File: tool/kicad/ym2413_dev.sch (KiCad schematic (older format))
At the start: 86 parts, among them P1 CONN_4, U1 YM2413, X1 CRYSTAL

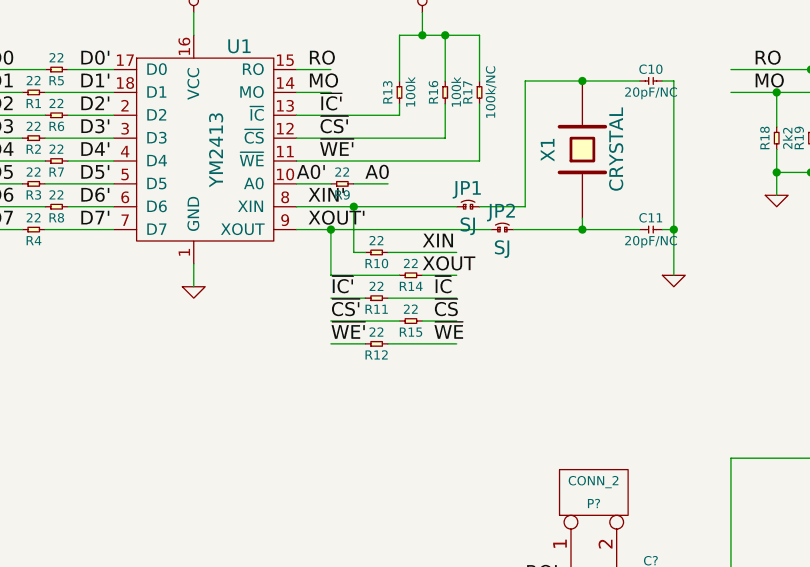
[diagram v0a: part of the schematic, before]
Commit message: add extra solder jumpers for XIN/XOUT handling on YM
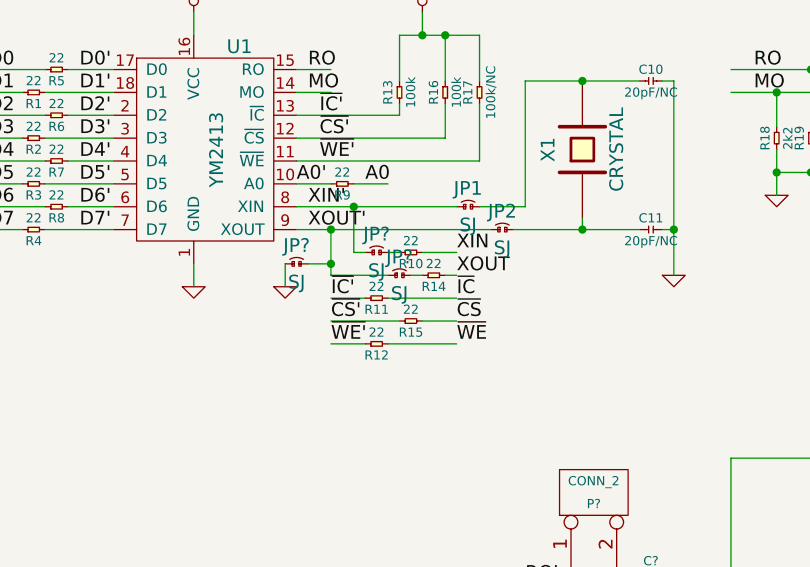
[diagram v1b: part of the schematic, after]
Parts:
- added JP? (x3): SJ, symbol SJ
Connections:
- wire segments 241 -> 245
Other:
- moved on the sheet: R10, R14
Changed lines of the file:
@@
 L R R10
 U 1 1 52E3BD6F
-P 6900 2400
-F 0 "R10" H 6900 2450 40  0000 C CNN
-F 1 "22" H 6900 2350 40  0000 C CNN
-F 2 "" H 6900 2400 60  0000 C CNN
-F 3 "" H 6900 2400 60  0000 C CNN
-	1    6900 2400
+P 7050 2400
+F 0 "R10" H 7050 2450 40  0000 C CNN
+F 1 "22" H 7050 2350 40  0000 C CNN
+F 2 "" H 7050 2400 60  0000 C CNN
+F 3 "" H 7050 2400 60  0000 C CNN
+	1    7050 2400
 	-1   0    0    1
 $EndComp
@@
 L R R14
 U 1 1 52E3BD75
-P 7050 2500
-F 0 "R14" H 7050 2550 40  0000 C CNN
-F 1 "22" H 7050 2450 40  0000 C CNN
-F 2 "" H 7050 2500 60  0000 C CNN
-F 3 "" H 7050 2500 60  0000 C CNN
-	1    7050 2500
+P 7150 2500
+F 0 "R14" H 7150 2550 40  0000 C CNN
+F 1 "22" H 7150 2450 40  0000 C CNN
+F 2 "" H 7150 2500 60  0000 C CNN
+F 3 "" H 7150 2500 60  0000 C CNN
+	1    7150 2500
 	-1   0    0    1
 $EndComp
-Text Label 7100 2400 0    60   ~ 0
+Text Label 7250 2400 0    60   ~ 0
 XIN
-Text Label 7100 2500 0    60   ~ 0
+Text Label 7250 2500 0    60   ~ 0
 XOUT
 $Comp
@@
 	-1   0    0    1
 $EndComp
-Text Label 7150 2600 0    60   ~ 0
+Text Label 7250 2600 0    60   ~ 0
 ~IC
-Text Label 7150 2700 0    60   ~ 0
+Text Label 7250 2700 0    60   ~ 0
 ~CS
-Text Label 7150 2800 0    60   ~ 0
+Text Label 7250 2800 0    60   ~ 0
 ~WE
 Text Label 6700 2800 0    60   ~ 0
@@
 	6950 2100 6800 2100
 Wire Wire Line
-	6850 2400 6800 2400
-Wire Wire Line
 	6800 2400 6800 2200
 Connection ~ 6800 2200
 Wire Wire Line
-	7000 2500 6700 2500
-Wire Wire Line
 	6700 2500 6700 2300
 Connection ~ 6700 2300
-Wire Wire Line
-	6950 2400 7250 2400
-Wire Wire Line
-	7250 2500 7100 2500
 Wire Wire Line
 	7250 2600 6950 2600
@@
 	4400 7350 4400 7400
 Connection ~ 4400 7400
+Wire Wire Line
+	7100 2400 7250 2400
+Wire Wire Line
+	7250 2500 7200 2500
+$Comp
+L SJ JP?
+U 1 1 52F78C85
+P 6900 2400
+F 0 "JP?" H 6900 2480 60  0000 C CNN
+F 1 "SJ" H 6900 2320 60  0000 C CNN
+F 2 "" H 6900 2400 60  0000 C CNN
+F 3 "" H 6900 2400 60  0000 C CNN
+	1    6900 2400
+	1    0    0    -1
+$EndComp
+$Comp
+L SJ JP?
+U 1 1 52F78C8B
+P 7000 2500
+F 0 "JP?" H 7000 2580 60  0000 C CNN
+F 1 "SJ" H 7000 2420 60  0000 C CNN
+F 2 "" H 7000 2500 60  0000 C CNN
+F 3 "" H 7000 2500 60  0000 C CNN
+	1    7000 2500
+	1    0    0    -1
+$EndComp
+Wire Wire Line
+	7100 2500 7050 2500
+Wire Wire Line
+	6950 2500 6700 2500
+Wire Wire Line
+	7000 2400 6950 2400
+Wire Wire Line
+	6850 2400 6800 2400
+$Comp
+L GND #PWR?
+U 1 1 52F7930D
+P 6500 2550
+F 0 "#PWR?" H 6500 2550 30  0001 C CNN
+F 1 "GND" H 6500 2480 30  0001 C CNN
+F 2 "" H 6500 2550 60  0000 C CNN
+F 3 "" H 6500 2550 60  0000 C CNN
+	1    6500 2550
+	1    0    0    -1
+$EndComp
+$Comp
+L SJ JP?
+U 1 1 52F79313
+P 6550 2450
+F 0 "JP?" H 6550 2530 60  0000 C CNN
+F 1 "SJ" H 6550 2370 60  0000 C CNN
+F 2 "" H 6550 2450 60  0000 C CNN
+F 3 "" H 6550 2450 60  0000 C CNN
+	1    6550 2450
+	1    0    0    -1
+$EndComp
+Wire Wire Line
+	6700 2450 6600 2450
+Connection ~ 6700 2450
+Wire Wire Line
+	6500 2450 6500 2550
 $EndSCHEMATC

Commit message: add SWC pull-up button to enable bootloader programming
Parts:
- added R?: 100, symbol R
- added S?: TACTSW, symbol TACTSW
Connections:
- wire segments 245 -> 249
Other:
- moved on the sheet: C?, P?, R?, U?

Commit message: add fast lvl shifer IC to make sure we provide a 5V clock on XI
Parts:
- removed P? (x2): CONN_2, symbol CONN_2
- added K?: CONN_3, symbol CONN_3
- added U?: SN74LVC2T45, symbol SN74LVC2T45
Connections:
- net labels added: XIN3V3, XOUT3V3
- wire segments 249 -> 268
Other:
- note added: "TODO: actual audio\nconnector"
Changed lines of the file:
@@
-$EndComp
-$Comp
-L CONN_2 P?
-U 1 1 52F742B0
-P 10650 3350
-F 0 "P?" V 10600 3350 40  0000 C CNN
-F 1 "CONN_2" V 10700 3350 40  0000 C CNN
-F 2 "" H 10650 3350 60  0000 C CNN
-F 3 "" H 10650 3350 60  0000 C CNN
-	1    10650 3350
-	1    0    0    -1
 $EndComp
 $Comp
@@
 $EndComp
 $Comp
-L CONN_2 P?
-U 1 1 52F7492B
-P 10650 4600
-F 0 "P?" V 10600 4600 40  0000 C CNN
-F 1 "CONN_2" V 10700 4600 40  0000 C CNN
-F 2 "" H 10650 4600 60  0000 C CNN
-F 3 "" H 10650 4600 60  0000 C CNN
-	1    10650 4600
-	1    0    0    -1
-$EndComp
-$Comp
 L GND #PWR?
 U 1 1 52F74931
@@
 	9950 3250 10050 3250
 Wire Wire Line
-	10150 3250 10300 3250
+	10150 3250 10400 3250
 Wire Wire Line
 	10200 3400 10200 3250
@@
 Wire Wire Line
 	8800 5550 8800 5650
+$Comp
+L CONN_3 K?
+U 1 1 52F7A1A7
+P 10850 3950
+F 0 "K?" V 10800 3950 50  0000 C CNN
+F 1 "CONN_3" V 10900 3950 40  0000 C CNN
+F 2 "" H 10850 3950 60  0000 C CNN
+F 3 "" H 10850 3950 60  0000 C CNN
+	1    10850 3950
+	1    0    0    -1
+$EndComp
+Wire Wire Line
+	10500 3850 10400 3850
+Wire Wire Line
+	10400 3850 10400 3250
+Wire Wire Line
+	10300 4500 10300 3950
+Wire Wire Line
+	10300 3950 10500 3950
+$Comp
+L GND #PWR?
+U 1 1 52F7A44E
+P 10400 4150
+F 0 "#PWR?" H 10400 4150 30  0001 C CNN
+F 1 "GND" H 10400 4080 30  0001 C CNN
+F 2 "" H 10400 4150 60  0000 C CNN
+F 3 "" H 10400 4150 60  0000 C CNN
+	1    10400 4150
+	1    0    0    -1
+$EndComp
+Wire Wire Line
+	10500 4050 10400 4050
+Wire Wire Line
+	10400 4050 10400 4150
+Text Notes 10700 5000 1    60   ~ 0
+TODO: actual audio\nconnector
+$Comp
+L SN74LVC2T45 U?
+U 1 1 52F7A857
+P 1450 4100
+F 0 "U?" H 1450 4450 60  0000 C CNN
+F 1 "SN74LVC2T45" H 1450 3800 60  0000 C CNN
+F 2 "" H 1500 3950 60  0000 C CNN
+F 3 "" H 1500 3950 60  0000 C CNN
+	1    1450 4100
+	-1   0    0    -1
+$EndComp
+$Comp
+L +3.3V #PWR?
+U 1 1 52F7A870
+P 1900 3750
+F 0 "#PWR?" H 1900 3710 30  0001 C CNN
+F 1 "+3.3V" H 1900 3860 30  0000 C CNN
+F 2 "" H 1900 3750 60  0000 C CNN
+F 3 "" H 1900 3750 60  0000 C CNN
+	1    1900 3750
+	1    0    0    -1
+$EndComp
+Wire Wire Line
+	1800 3900 1900 3900
+Wire Wire Line
+	1900 3750 1900 4000
+Wire Wire Line
+	1900 4000 1800 4000
+Connection ~ 1900 3900
+Wire Wire Line
+	1800 4100 2000 4100
+Wire Wire Line
+	2000 4100 2000 3900
+Wire Wire Line
+	2000 3900 2850 3900
+Wire Wire Line
+	1800 4200 2050 4200
+Wire Wire Line
+	2050 4200 2050 4000
+Wire Wire Line
+	2050 4000 2850 4000
+Wire Wire Line
+	950  4100 1100 4100
+Wire Wire Line
+	950  4200 1100 4200
+Wire Wire Line
+	1100 3900 950  3900
+Wire Wire Line
+	950  3900 950  3800
+$Comp
+L +5V #PWR?
+U 1 1 52F7B2D9
+P 950 3800
+F 0 "#PWR?" H 950 3890 20  0001 C CNN
+F 1 "+5V" H 950 3890 30  0000 C CNN
+F 2 "" H 950 3800 60  0000 C CNN
+F 3 "" H 950 3800 60  0000 C CNN
+	1    950  3800
+	1    0    0    -1
+$EndComp
+Text Label 1000 4100 2    60   ~ 0
+XIN
+Text Label 1000 4200 2    60   ~ 0
+XOUT
+Text Label 2050 3900 0    60   ~ 0
+XIN3V3
+Text Label 2050 4000 0    60   ~ 0
+XOUT3V3
 $EndSCHEMATC

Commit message: cleanup; assign pins; add test points; restart pcb layout from zero
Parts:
- added D1, D10, D11, D2, D3, D4, D5, D6, D7, D8, D9: LED, symbol LED
- added K1: CONN_3, symbol CONN_3
- added P1, P10, P11, P12, P13, P14, P15, P16, P17, P18, P19, P2, P20, P21, P22, P23, P24, P25, P26, P27, P28, P29, P3, P33, P34, P4, P6, P7, P8, P9: TEST_POINT, symbol TEST_POINT
- added R1, R10, R13, R2, R3, R4, R5, R6, R7, R8, R9: 3k3, symbol R
- added R25, R26, R27: 22, symbol R
- IC1: renamed from IC?; footprint DIP8 -> (none)
- P5: renamed from P?; value MINI-IN -> MIDI-IN
- gave numbers to parts that had none: 55
- renumbered C10 to C15, C11 to C16, C1 to C18, C2 to C19, JP1 to JP4, JP2 to JP5, P1 to P35, R1 to R17, R2 to R18, R3 to R19, R4 to R20, R5 to R21, R6 to R22, R7 to R23, R8 to R24, R9 to R28, R11 to R29, R12 to R30, R13 to R31, R10 to R32, R15 to R33, R14 to R34, R16 to R35, R17 to R36, R18 to R40, R19 to R41, R20 to R43, R21 to R44, R22 to R45, R23 to R46, R24 to R47, R25 to R50, U1 to U4, X1 to X2
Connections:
- net labels added: DEBUG_RX, DEBUG_TX, LED0, LED1, LED2, LED3, LED4, LED5, LED6, LED7, LED8, LED9, USB_DMPU
- wire segments 268 -> 351
- no-connect marks 3 -> 4

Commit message: add 6-pin FTDI debug header
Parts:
- removed P35: CONN_4, symbol CONN_4
- added P35: CONN_6, symbol CONN_6
- added P36: CONN_5, symbol CONN_5
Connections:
- net labels added: RXI, TXO
- wire segments 351 -> 360
- no-connect marks 4 -> 5
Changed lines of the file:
@@
 MO/2
 $Comp
-L CONN_4 P35
-U 1 1 52E3A865
-P 10750 1750
-F 0 "P35" V 10700 1750 50  0000 C CNN
-F 1 "CONN_4" V 10800 1750 50  0000 C CNN
-F 2 "" H 10750 1750 60  0000 C CNN
-F 3 "" H 10750 1750 60  0000 C CNN
-	1    10750 1750
-	1    0    0    -1
-$EndComp
-$Comp
 L R R40
 U 1 1 52E3AC6B
@@
 	0    -1   -1   0
 $EndComp
+$Comp
+L CONN_5 P36
+U 1 1 52F868F0
+P 10800 1700
+F 0 "P36" V 10750 1700 50  0000 C CNN
+F 1 "CONN_5" V 10850 1700 50  0000 C CNN
+F 2 "" H 10800 1700 60  0000 C CNN
+F 3 "" H 10800 1700 60  0000 C CNN
+	1    10800 1700
+	1    0    0    -1
+$EndComp
+Wire Wire Line
+	10400 1500 10350 1500
+Wire Wire Line
+	10350 1500 10350 1900
+Connection ~ 10350 1900
+$Comp
+L CONN_6 P35
+U 1 1 52F86C85
+P 6400 6700
+F 0 "P35" V 6350 6700 60  0000 C CNN
+F 1 "CONN_6" V 6450 6700 60  0000 C CNN
+F 2 "" H 6400 6700 60  0000 C CNN
+F 3 "" H 6400 6700 60  0000 C CNN
+	1    6400 6700
+	1    0    0    -1
+$EndComp
+Wire Wire Line
+	6050 6450 6000 6450
+Wire Wire Line
+	6000 6450 6000 6850
+Wire Wire Line
+	6000 6850 6050 6850
+Wire Wire Line
+	5600 6550 6050 6550
+Wire Wire Line
+	5600 6650 6050 6650
+Wire Wire Line
+	5900 6950 6050 6950
+$Comp
+L GND #PWR056
+U 1 1 52F8750B
+P 5900 7050
+F 0 "#PWR056" H 5900 7050 30  0001 C CNN
+F 1 "GND" H 5900 6980 30  0001 C CNN
+F 2 "" H 5900 7050 60  0000 C CNN
+F 3 "" H 5900 7050 60  0000 C CNN
+	1    5900 7050
+	1    0    0    -1
+$EndComp
+Wire Wire Line
+	5900 6950 5900 7050
+NoConn ~ 6050 6750
+Text Label 5950 6650 2    60   ~ 0
+TXO
+Text Label 5950 6550 2    60   ~ 0
+RXI
+Text Label 5750 6550 2    60   ~ 0
+DEBUG_TX
+Text Label 5750 6650 2    60   ~ 0
+DEBUG_RX
 $EndSCHEMATC

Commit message: rough layout
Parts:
- removed R29, R30, R33: 22, symbol R
- added P37, P38: TEST_POINT, symbol TEST_POINT
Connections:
- net labels added: MOA, MOA2, MOA3, MOI2, ROA, ROA2, ROA3, ROI2
- wire segments 360 -> 362
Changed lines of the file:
@@
 XOUT
-$Comp
-L R R29
-U 1 1 52E3BF37
-P 6900 2600
-F 0 "R29" H 6900 2650 40  0000 C CNN
-F 1 "22" H 6900 2550 40  0000 C CNN
-F 2 "" H 6900 2600 60  0000 C CNN
-F 3 "" H 6900 2600 60  0000 C CNN
-	1    6900 2600
-	-1   0    0    1
-$EndComp
-$Comp
-L R R33
-U 1 1 52E3BFF3
-P 7050 2700
-F 0 "R33" H 7050 2750 40  0000 C CNN
-F 1 "22" H 7050 2650 40  0000 C CNN
-F 2 "" H 7050 2700 60  0000 C CNN
-F 3 "" H 7050 2700 60  0000 C CNN
-	1    7050 2700
-	-1   0    0    1
-$EndComp
-$Comp
-L R R30
-U 1 1 52E3BFF9
-P 6900 2800
-F 0 "R30" H 6900 2850 40  0000 C CNN
-F 1 "22" H 6900 2750 40  0000 C CNN
-F 2 "" H 6900 2800 60  0000 C CNN
-F 3 "" H 6900 2800 60  0000 C CNN
-	1    6900 2800
-	-1   0    0    1
-$EndComp
-Text Label 7250 2600 0    60   ~ 0
-~IC
-Text Label 7250 2700 0    60   ~ 0
-~CS
-Text Label 7250 2800 0    60   ~ 0
-~WE
-Text Label 6700 2800 0    60   ~ 0
-~WE'
-Text Label 6700 2700 0    60   ~ 0
-~CS'
-Text Label 6700 2600 0    60   ~ 0
-~IC'
 $Comp
 L SJ JP5
@@
 L +3.3VADC #PWR014
 U 1 1 52F431B2
-P 3450 2450
-F 0 "#PWR014" H 3450 2570 20  0001 C CNN
-F 1 "+3.3VADC" H 3450 2540 30  0000 C CNN
-F 2 "" H 3450 2450 60  0000 C CNN
-F 3 "" H 3450 2450 60  0000 C CNN
-	1    3450 2450
+P 3450 2500
+F 0 "#PWR014" H 3450 2620 20  0001 C CNN
+F 1 "+3.3VADC" H 3450 2590 30  0000 C CNN
+F 2 "" H 3450 2500 60  0000 C CNN
+F 3 "" H 3450 2500 60  0000 C CNN
+	1    3450 2500
 	1    0    0    -1
 $EndComp
@@
 F 3 "" H 2800 6700 60  0000 C CNN
 	1    2800 6700
-	1    0    0    -1
+	-1   0    0    1
 $EndComp
 NoConn ~ 1600 6750
@@
 	1    0    0    -1
 $EndComp
-Text Label 3600 6650 0    60   ~ 0
+Text Label 3950 6500 1    60   ~ 0
 D-
-Text Label 3600 6750 0    60   ~ 0
+Text Label 4050 6500 1    60   ~ 0
 D+
 $Comp
@@
 Text Label 1850 6400 0    60   ~ 0
 VBUS_IN
-Text Label 1850 6650 0    60   ~ 0
+Text Label 2150 6750 0    60   ~ 0
 D-_IN
-Text Label 1900 6700 3    60   ~ 0
+Text Label 2150 6650 0    60   ~ 0
 D+_IN
 Text Label 1650 7050 1    60   ~ 0
@@
 	1    0    0    -1
 $EndComp
+Text Label 3150 6750 0    60   ~ 0
+D-B
 Text Label 3150 6650 0    60   ~ 0
-D-B
-Text Label 3150 6750 0    60   ~ 0
 D+B
 $Comp
@@
 Connection ~ 6700 2300
 Wire Wire Line
-	7250 2600 6950 2600
-Wire Wire Line
-	7250 2700 7100 2700
-Wire Wire Line
-	7250 2800 6950 2800
-Wire Wire Line
-	6850 2600 6700 2600
-Wire Wire Line
-	6700 2700 7000 2700
-Wire Wire Line
-	6700 2800 6850 2800
-Wire Wire Line
 	3250 5850 3250 5600
 Wire Wire Line
@@
 	1650 7250 1650 7300
 Wire Wire Line
-	1600 6650 2450 6650
-Wire Wire Line
-	1600 6700 2400 6700
-Wire Wire Line
-	2400 6700 2400 6750
-Wire Wire Line
-	2400 6750 2450 6750
-Wire Wire Line
 	1700 6400 1700 6600
 Wire Wire Line
@@
 	1700 6400 3050 6400
 Wire Wire Line
-	2750 6400 2750 6450
-Wire Wire Line
-	2850 6950 2850 7050
-Wire Wire Line
 	3150 6650 3350 6650
 Wire Wire Line
@@
 Wire Wire Line
 	3300 6400 3150 6400
-Connection ~ 2750 6400
 Wire Wire Line
 	3300 6350 3300 6400
-Wire Wire Line
-	3450 6650 4050 6650
-Wire Wire Line
-	3550 6750 3950 6750
 Wire Wire Line
 	4050 2900 4050 2450
@@
 Connection ~ 1900 3900
 Wire Wire Line
-	1800 4100 2000 4100
-Wire Wire Line
-	2000 4100 2000 3900
+	2000 3900 2000 4200
 Wire Wire Line
 	2000 3900 2850 3900
 Wire Wire Line
-	1800 4200 2050 4200
-Wire Wire Line
-	2050 4200 2050 4000
-Wire Wire Line
-	2050 4000 2850 4000
+	1950 4000 2850 4000
 Wire Wire Line
 	950  4100 1100 4100
@@
 	1    0    0    -1
 $EndComp
-Text Label 1000 4100 2    60   ~ 0
+Text Label 950  4200 2    60   ~ 0
 XIN
-Text Label 1000 4200 2    60   ~ 0
+Text Label 950  4100 2    60   ~ 0
 XOUT
 Text Label 2050 3900 0    60   ~ 0
@@
 Text Label 5750 6650 2    60   ~ 0
 DEBUG_RX
+Text Label 8250 3150 0    60   ~ 0
+ROI2
+Text Label 8200 3900 0    60   ~ 0
+MOI2
+Text Label 9500 3700 0    60   ~ 0
+ROA
+Text Label 9500 4950 0    60   ~ 0
+MOA
+Text Label 10000 3250 1    60   ~ 0
+ROA2
+Text Label 10000 4500 1    60   ~ 0
+MOA2
+Text Label 10300 4300 1    60   ~ 0
+MOA3
+Text Label 10400 3600 1    60   ~ 0
+ROA3
+Wire Wire Line
+	2000 4200 1800 4200
+Wire Wire Line
+	1950 4000 1950 4100
+Wire Wire Line
+	1950 4100 1800 4100
+$Comp
+L GND #PWR057
+U 1 1 52F8A394
+P 1850 4400
+F 0 "#PWR057" H 1850 4400 30  0001 C CNN
+F 1 "GND" H 1850 4330 30  0001 C CNN
+F 2 "" H 1850 4400 60  0000 C CNN
+F 3 "" H 1850 4400 60  0000 C CNN
+	1    1850 4400
+	1    0    0    -1
+$EndComp
+Wire Wire Line
+	1800 4300 1850 4300
+Wire Wire Line
+	1850 4300 1850 4400
+Wire Wire Line
+	2850 6950 2600 6950
+Wire Wire Line
+	2600 6950 2600 6400
+Connection ~ 2600 6400
+Wire Wire Line
+	2750 6450 2900 6450
+Wire Wire Line
+	2900 6450 2900 7000
+Wire Wire Line
+	2900 7000 2850 7000
+Wire Wire Line
+	2850 7000 2850 7050
+Wire Wire Line
+	3450 6650 4050 6650
+Wire Wire Line
+	3950 6750 3550 6750
+Wire Wire Line
+	2450 6650 2050 6650
+Wire Wire Line
+	2050 6650 2050 6700
+Wire Wire Line
+	2050 6700 1600 6700
+Wire Wire Line
+	1600 6650 1950 6650
+Wire Wire Line
+	1950 6650 1950 6750
+Wire Wire Line
+	1950 6750 2450 6750
+$Comp
+L TEST_POINT P37
+U 1 1 52F8B72C
+P 6700 1600
+F 0 "P37" H 6875 1600 40  0000 C CNN
+F 1 "TEST_POINT" H 6700 1350 60  0001 C CNN
+F 2 "" H 6700 1600 60  0000 C CNN
+F 3 "" H 6700 1600 60  0000 C CNN
+	1    6700 1600
+	1    0    0    -1
+$EndComp
+$Comp
+L TEST_POINT P38
+U 1 1 52F8B732
+P 6700 1700
+F 0 "P38" H 6875 1700 40  0000 C CNN
+F 1 "TEST_POINT" H 6700 1450 60  0001 C CNN
+F 2 "" H 6700 1700 60  0000 C CNN
+F 3 "" H 6700 1700 60  0000 C CNN
+	1    6700 1700
+	1    0    0    -1
+$EndComp
 $EndSCHEMATC
